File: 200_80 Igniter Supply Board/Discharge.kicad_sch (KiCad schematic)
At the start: 13 parts, among them J4 112659, J6 MMCX, U10 OP37

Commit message: Rebasing
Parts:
- removed C51: 100n, Capacitor_SMD:C_0603_1608Metric, symbol Device:C
- removed D18: BAT54WS, Diode_SMD:D_SOD-323, symbol Device:D_Schottky
- removed J4: 112659, 0_PAY_Footprint_Library:CONN_112659, symbol Connector:Conn_01x02_Pin
- removed R22: 3.74k 1%, Resistor_SMD:R_0603_1608Metric, symbol Device:R
- removed R24: 100, Resistor_SMD:R_0603_1608Metric, symbol Device:R
- added C50: 500pF, Capacitor_SMD:C_0603_1608Metric_Pad1.08x0.95mm_HandSolder, symbol Device:C
- added D20: BAT54L, Package_TO_SOT_SMD:SOT-23-3, symbol Device:D_Schottky
- added J4: BNC, 0_PAY_Footprint_Library:CONN_112659, symbol Connector:Conn_Coaxial
- added R25: 50R, Resistor_SMD:R_0603_1608Metric_Pad0.98x0.95mm_HandSolder, symbol Device:R_US
- C1, C3: value 100n -> 100nF
- U10: Digikey PN (none) -> OP37GSZ
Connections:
- net DISCHARGE_V is gone; now on net AMP_OUT: D19.1 (K), J6.1 (In)
- net AMP_OUT: now also D20.3 (K), R25.1
- net DISCHARGE_HV: now also J4.1 (In)
- net GND: now also U10.3 (+), C50.2, D20.1 (A), J4.2 (Ext)
- new net: C50.1, R25.2
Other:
- note removed: "noise gain 6"

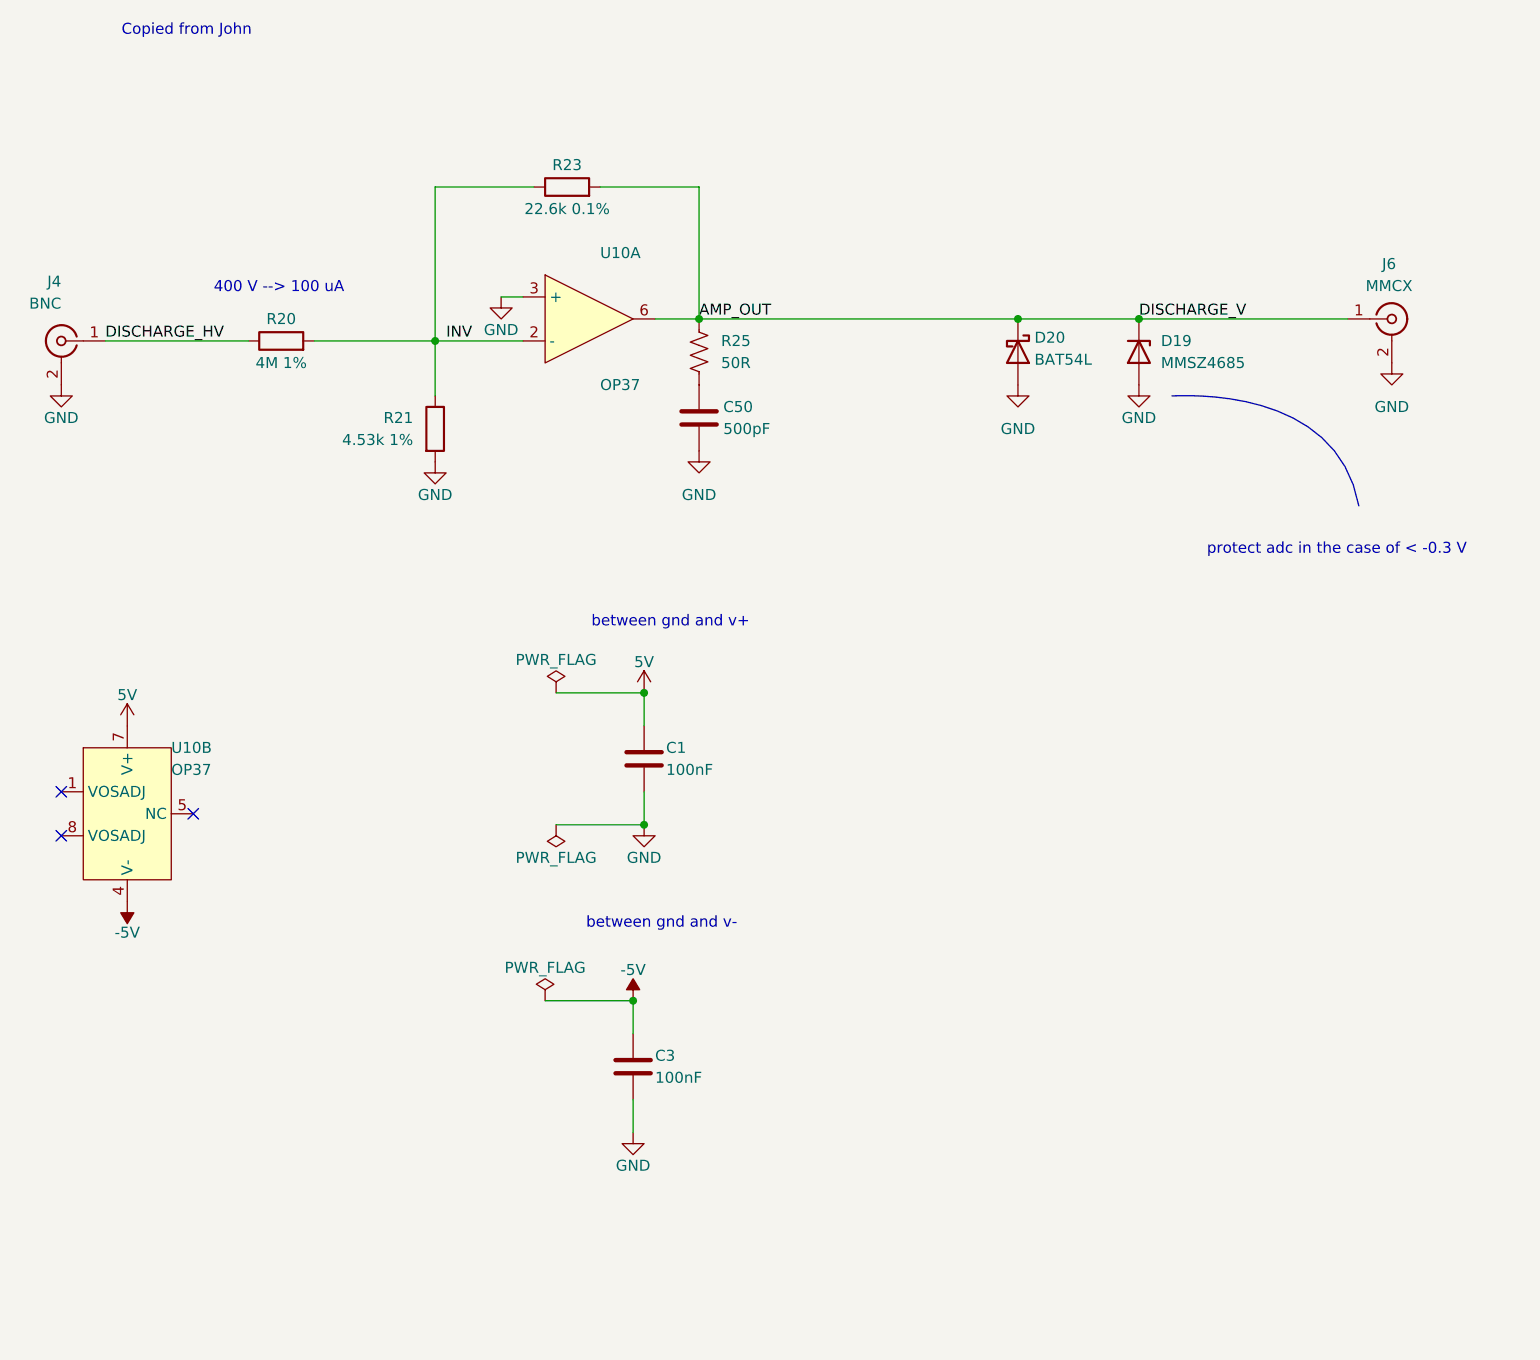
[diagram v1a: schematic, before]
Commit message: Schematic updates
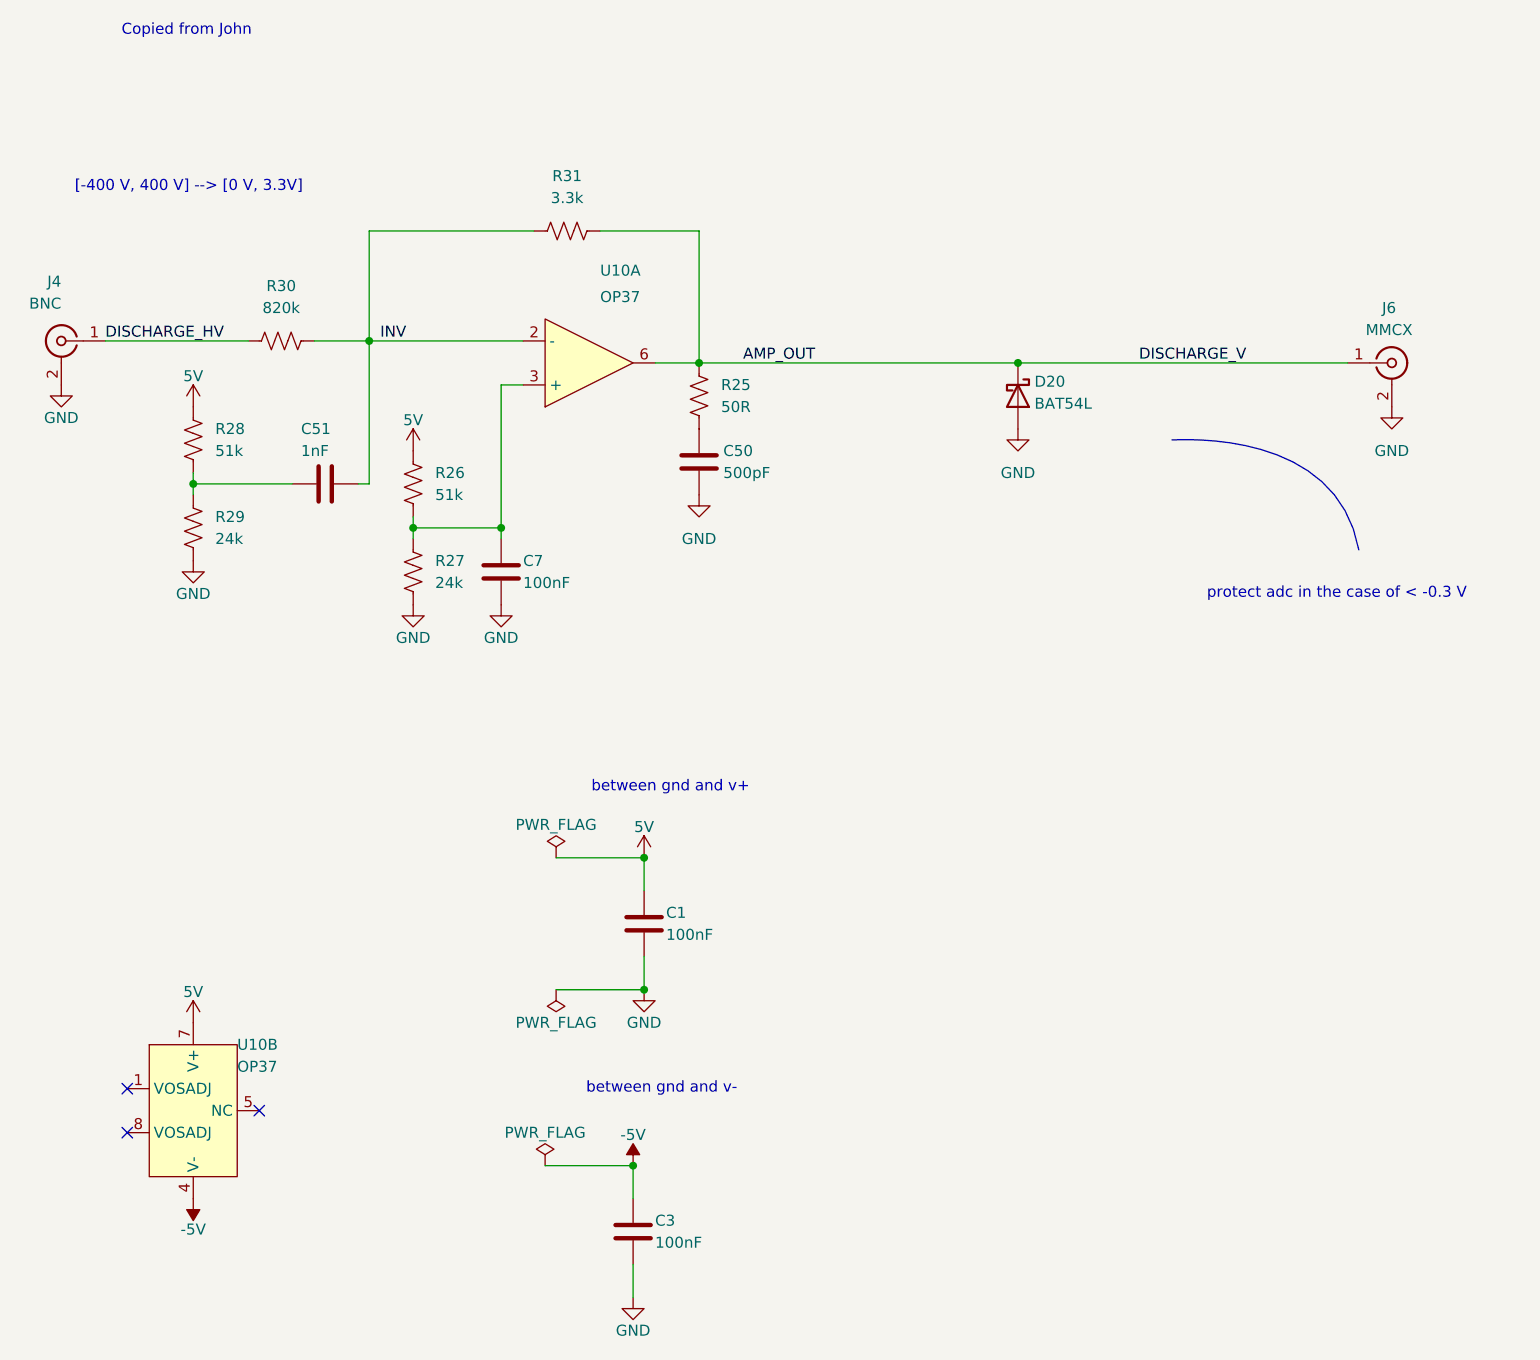
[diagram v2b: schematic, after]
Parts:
- removed D19: MMSZ4685, Diode_SMD:D_SOD-123, symbol Device:D_Zener
- removed R20: 4M 1%, Resistor_SMD:R_2512_6332Metric, symbol Device:R
- removed R21: 4.53k 1%, Resistor_SMD:R_0603_1608Metric, symbol Device:R
- removed R23: 22.6k 0.1%, Resistor_SMD:R_0603_1608Metric, symbol Device:R
- added C51: 1nF, Capacitor_SMD:C_0603_1608Metric, symbol Device:C
- added C7: 100nF, Capacitor_SMD:C_0603_1608Metric, symbol Device:C
- added R26, R28: 51k, Resistor_SMD:R_0603_1608Metric_Pad0.98x0.95mm_HandSolder, symbol Device:R_US
- added R27, R29: 24k, Resistor_SMD:R_0603_1608Metric_Pad0.98x0.95mm_HandSolder, symbol Device:R_US
- added R30: 820k, Resistor_SMD:R_2512_6332Metric, symbol Device:R_US
- added R31: 3.3k, Resistor_SMD:R_0603_1608Metric_Pad0.98x0.95mm_HandSolder, symbol Device:R_US
- C1, C3: Digikey PN (none) -> 399-C0603C104K5RACTUCT-ND
- C50: Digikey PN (none) -> 13-CC0603JRNPO9BN501CT-ND
- D20: Digikey PN BAT54LT1G -> BAT54LT1GOSCT-ND
- J4: Digikey PN 112659 -> 115-112659-ND
- J6: Digikey PN (none) -> WM5557-ND
- R25: Digikey PN (none) -> 541-3318-1-ND
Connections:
- net 5V: now also R26.1, R28.1
- net AMP_OUT: now also R31.2
- net DISCHARGE_HV: now also R30.1
- net GND: now also C7.2, R27.2, R29.2; no longer U10.3 (+)
- net INV: now also C51.2, R30.2, R31.1
- new net: C51.1, R28.2, R29.1
- new net: C7.1, R26.2, R27.1, U10.3 (+)
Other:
- note added: "[-400 V, 400 V] --> [0 V, 3.3V]"
- note removed: "400 V --> 100 uA"
- moved on the sheet: C1, C3, C50, D20, J6, R25, U10A, U10B

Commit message: Layout update
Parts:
- C1, C3, C7: footprint Capacitor_SMD:C_0603_1608Metric -> Capacitor_SMD:C_0603_1608Metric_Pad1.08x0.95mm_HandSolder
- C51: footprint Capacitor_SMD:C_0603_1608Metric -> Capacitor_SMD:C_0603_1608Metric_Pad1.08x0.95mm_HandSolder; Digikey PN 399-C0603C104K5RACTUCT-ND -> 399-C0603C102F3GACTUCT-ND
- R26, R28: Digikey PN 541-3318-1-ND -> RR08P51.0KDCT-ND
- R27, R29: Digikey PN 541-3318-1-ND -> RG16P24.0KBCT-ND
- R30: Digikey PN 541-3318-1-ND -> A130028CT-ND
- R31: Digikey PN 541-3318-1-ND -> P123763CT-ND
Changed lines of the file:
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@@
 	)
 	(junction
+		(at 124.46 177.8)
+		(diameter 0)
+		(color 0 0 0 0)
+	)
+	(junction
 		(at 125.73 127)
 		(diameter 0)
@@
 	(wire
 		(pts
+			(xy 124.46 177.8) (xy 114.3 177.8)
+		)
+		(stroke
+			(width 0)
+			(type default)
+		)
+	)
+	(wire
+		(pts
 			(xy 124.46 173.99) (xy 124.46 177.8)
 		)
@@
 			)
 		)
-		(property "Footprint" "Capacitor_SMD:C_0603_1608Metric"
+		(property "Footprint" "Capacitor_SMD:C_0603_1608Metric_Pad1.08x0.95mm_HandSolder"
 			(at 88.9 83.82 0)
 			(hide yes)
@@
 			)
 		)
-		(property "Digikey PN" "399-C0603C104K5RACTUCT-ND"
+		(property "Digikey PN" "399-C0603C102F3GACTUCT-ND"
 			(at 88.9 83.82 0)
 			(hide yes)
@@
 			)
 		)
-		(property "Digikey PN" "541-3318-1-ND"
+		(property "Digikey PN" "RG16P24.0KBCT-ND"
 			(at 99.06 93.98 0)
 			(hide yes)
@@
 			)
 		)
-		(property "Digikey PN" "541-3318-1-ND"
+		(property "Digikey PN" "RG16P24.0KBCT-ND"
 			(at 73.66 88.9 0)
 			(hide yes)
@@
 			)
 		)
-		(property "Digikey PN" "541-3318-1-ND"
+		(property "Digikey PN" "RR08P51.0KDCT-ND"
 			(at 99.06 83.82 0)
 			(hide yes)
@@
 			)
 		)
-		(property "Footprint" "Capacitor_SMD:C_0603_1608Metric"
+		(property "Footprint" "Capacitor_SMD:C_0603_1608Metric_Pad1.08x0.95mm_HandSolder"
 			(at 124.46 170.18 0)
 			(hide yes)
@@
 			)
 		)
-		(property "Footprint" "Capacitor_SMD:C_0603_1608Metric"
+		(property "Footprint" "Capacitor_SMD:C_0603_1608Metric_Pad1.08x0.95mm_HandSolder"
 			(at 109.22 93.98 0)
 			(hide yes)
@@
 			)
 		)
-		(property "Digikey PN" "541-3318-1-ND"
+		(property "Digikey PN" "RR08P51.0KDCT-ND"
 			(at 73.66 78.74 0)
 			(hide yes)
@@
 			)
 		)
-		(property "Digikey PN" "541-3318-1-ND"
+		(property "Digikey PN" "A130028CT-ND"
 			(at 83.82 67.31 0)
 			(hide yes)
@@
 	)
 	(symbol
+		(lib_id "power:PWR_FLAG")
+		(at 114.3 177.8 180)
+		(unit 1)
+		(body_style 1)
+		(exclude_from_sim no)
+		(in_bom no)
+		(on_board no)
+		(in_pos_files no)
+		(dnp no)
+		(property "Reference" "#FLG015"
+			(at 114.3 172.72 0)
+			(hide yes)
+			(show_name no)
+			(do_not_autoplace no)
+			(effects
+				(font
+					(size 1.27 1.27)
+				)
+			)
+		)
+		(property "Value" "PWR_FLAG"
+			(at 114.3 181.61 0)
+			(show_name no)
+			(do_not_autoplace no)
+			(effects
+				(font
+					(size 1.27 1.27)
+				)
+			)
+		)
+		(property "Footprint" ""
+			(at 114.3 177.8 0)
+			(hide yes)
+			(show_name no)
+			(do_not_autoplace no)
+			(effects
+				(font
+					(size 1.27 1.27)
+				)
+			)
+		)
+		(property "Datasheet" ""
+			(at 114.3 177.8 0)
+			(hide yes)
+			(show_name no)
+			(do_not_autoplace no)
+			(effects
+				(font
+					(size 1.27 1.27)
+				)
+			)
+		)
+		(property "Description" ""
+			(at 114.3 177.8 0)
+			(hide yes)
+			(show_name no)
+			(do_not_autoplace no)
+			(effects
+				(font
+					(size 1.27 1.27)
+				)
+			)
+		)
+		(pin "1"
+		)
+		(instances
+			(project "Igniter Supply Board"
+				(path "/0667bf65-916d-41a8-8a49-6f64c5a5f247/273ee1b0-9086-4acc-845c-b41ea2be318e"
+					(reference "#FLG015")
+					(unit 1)
+				)
+			)
+		)
+	)
+	(symbol
 		(lib_id "Device:R_US")
 		(at 116.84 54.61 90)
@@
 			)
 		)
-		(property "Digikey PN" "541-3318-1-ND"
+		(property "Digikey PN" "P123763CT-ND"
 			(at 116.84 54.61 0)
 			(hide yes)
@@
 			)
 		)
-		(property "Footprint" "Capacitor_SMD:C_0603_1608Metric"
+		(property "Footprint" "Capacitor_SMD:C_0603_1608Metric_Pad1.08x0.95mm_HandSolder"
 			(at 125.73 134.62 0)
 			(hide yes)

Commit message: Final changes question mark
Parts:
- removed R29: 24k, Resistor_SMD:R_0603_1608Metric_Pad0.98x0.95mm_HandSolder, symbol Device:R_US
- R28: value 51k -> 1k; Digikey PN RR08P51.0KDCT-ND -> 2019-RK73H1JTTD1001FCT-ND
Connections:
- net 5V: no longer R28.1
- net GND: now also C51.1
- net INV: now also R28.1; no longer C51.2
- net at R28.2: now also C51.2; no longer C51.1
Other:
- moved on the sheet: R28

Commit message: Final changes question mark :pray:
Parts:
- R28: Digikey PN 2019-RK73H1JTTD1001FCT-ND -> RNCF0603BTE1K00
- U10: Digikey PN OP37GSZ -> 505-OP37GSZ-ND
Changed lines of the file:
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@@
 			)
 		)
-		(property "Digikey PN" "OP37GSZ"
+		(property "Digikey PN" "505-OP37GSZ-ND"
 			(at 118.11 74.93 0)
 			(hide yes)
@@
 			)
 		)
-		(property "Digikey PN" "OP37GSZ"
+		(property "Digikey PN" "505-OP37GSZ-ND"
 			(at 73.66 146.05 0)
 			(hide yes)
@@
 			)
 		)
-		(property "Digikey PN" "2019-RK73H1JTTD1001FCT-ND"
+		(property "Digikey PN" "RNCF0603BTE1K00"
 			(at 83.82 83.82 0)
 			(hide yes)
